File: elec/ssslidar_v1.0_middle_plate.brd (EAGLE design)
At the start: 15 x 15 mm, 6 parts

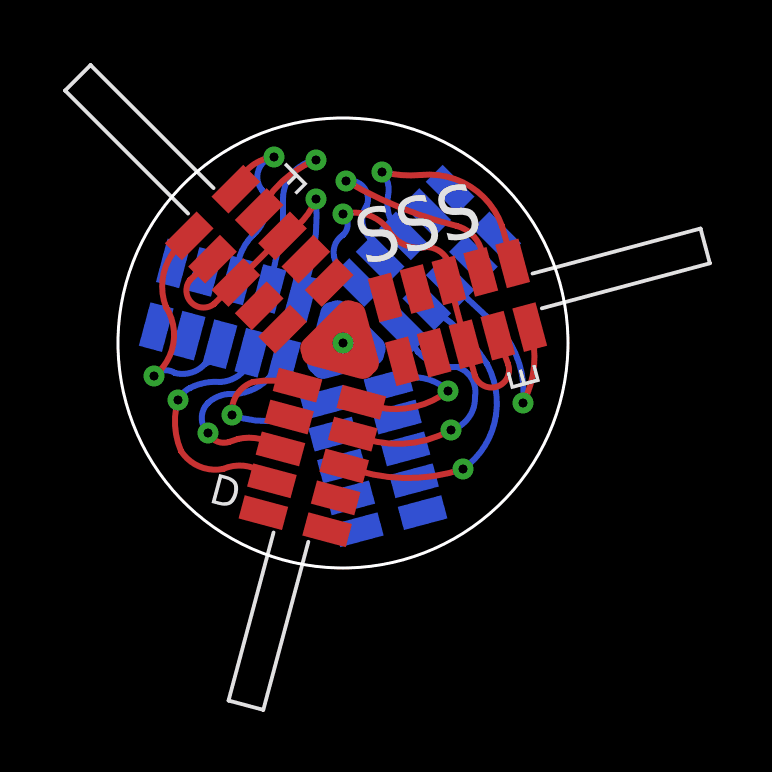
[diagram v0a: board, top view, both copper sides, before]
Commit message: Upadted blade footprint, put everything in v1.0
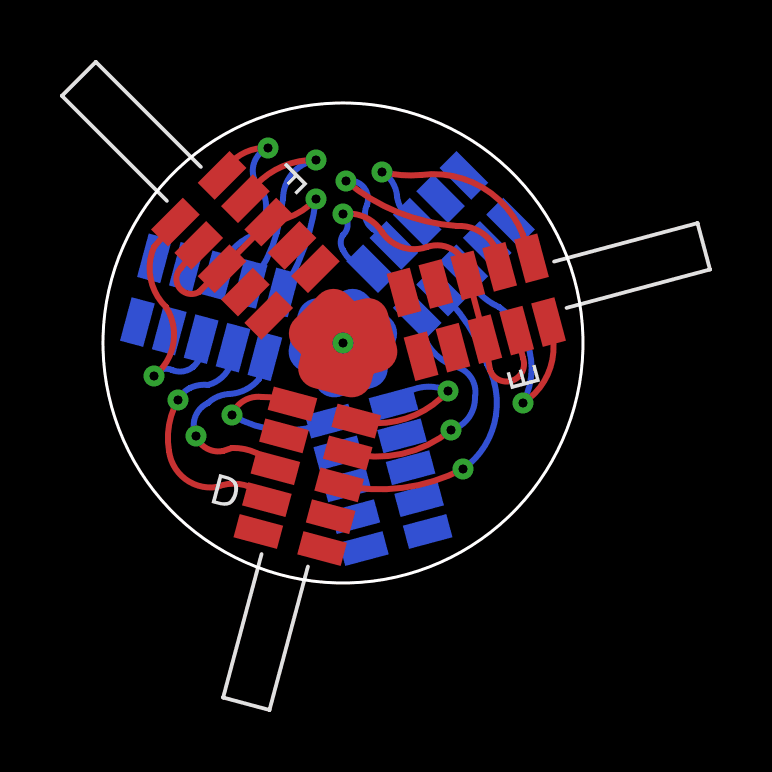
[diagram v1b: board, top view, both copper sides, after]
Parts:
- added U$1: (no value), Xevelabs:XEVELABS_LOGO_S
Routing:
- net GND: track 5.47 -> 7.92 mm
- net N$4: track 5.97 -> 6.50 mm
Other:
- board size 15 x 15 mm -> 16 x 16 mm
- board text added: "A"
- board text added: "B"
- board text added: "C"
- board text removed: "SSS"

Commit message: Updated all libs.
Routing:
- net GND: vias 1 -> 4
- added copper zone on layer 2, net GND
- added copper zone on layer 3, net VDD
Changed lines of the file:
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@@
 <wire x1="8" y1="8.353553125" x2="8" y2="8" width="0.2" layer="16"/>
 <wire x1="7.780003125" y1="7.1789625" x2="8.1294125" y2="7.517034375" width="0.2" layer="1"/>
+<polygon width="0.15" layer="2">
+<vertex x="-3" y="17.2"/>
+<vertex x="17.9" y="17.2"/>
+<vertex x="17.9" y="-1"/>
+<vertex x="-2.3" y="-1"/>
+</polygon>
+<via x="6.9" y="15.1" extent="1-16" drill="0.3"/>
+<via x="13.6" y="3.9" extent="1-16" drill="0.3"/>
+<via x="1.3" y="5.6" extent="1-16" drill="0.3"/>
 </signal>
 <signal name="VDD">
@@
 <wire x1="4.3" y1="5.6" x2="5.3" y2="6.2" width="0.2" layer="1" curve="-77.033827"/>
 <wire x1="5.3" y1="6.2" x2="6.316315625" y2="5.966478125" width="0.2" layer="1" curve="-29.379539"/>
+<polygon width="0.15" layer="3">
+<vertex x="-1.8" y="17"/>
+<vertex x="17.8" y="17.2"/>
+<vertex x="17.8" y="-1"/>
+<vertex x="-2.4" y="-1"/>
+</polygon>
 </signal>
 <signal name="N$1">
